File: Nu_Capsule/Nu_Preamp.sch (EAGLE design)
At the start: 27 parts, among them Q1 2SC3324, Q2 2SC3324, U1 TLV170

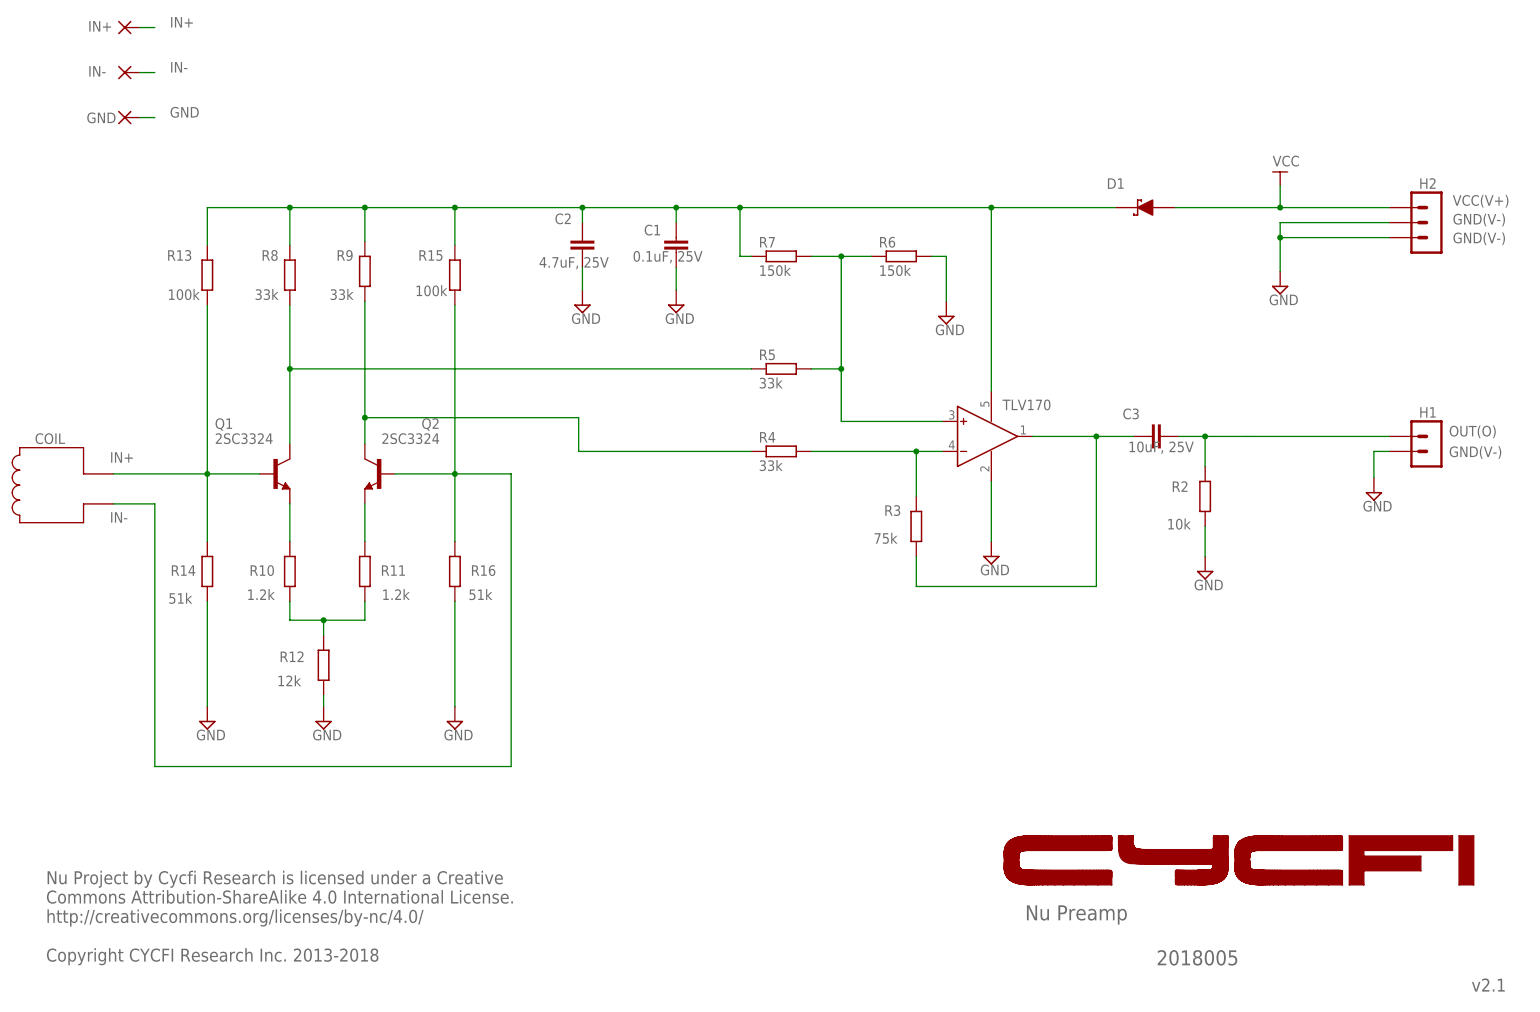
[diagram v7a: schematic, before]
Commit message: Remove commas and voltage rating on capacitor symbols on schematics
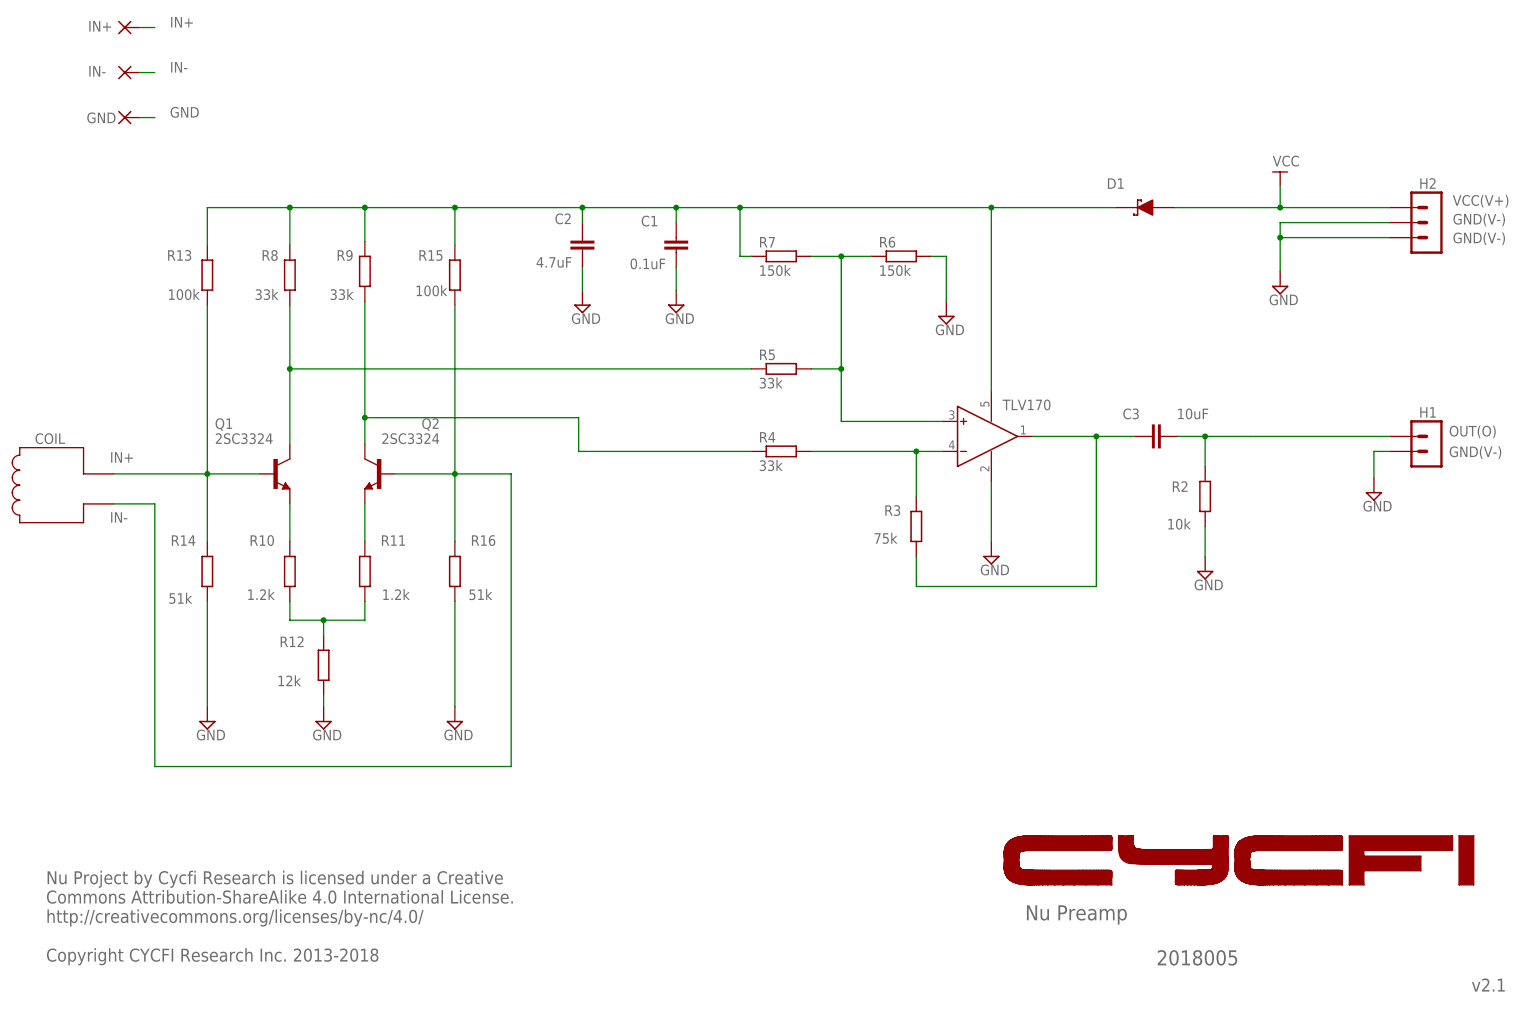
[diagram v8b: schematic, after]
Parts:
- C1: value 0.1uF, 25V -> 0.1uF
- C2: value 4.7uF, 25V -> 4.7uF
- C3: value 10uF, 25V -> 10uF
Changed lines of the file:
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@@
 <part name="SUPPLY10" library="supply2" deviceset="GND" device=""/>
 <part name="D1" library="m-pad-2.1" deviceset="D_SCHOTTKY" device="L"/>
-<part name="C1" library="rcl" deviceset="C-EU" device="C0402" value="0.1uF, 25V"/>
+<part name="C1" library="rcl" deviceset="C-EU" device="C0402" value="0.1uF"/>
 <part name="SUPPLY11" library="supply2" deviceset="GND" device=""/>
 <part name="SUPPLY12" library="supply2" deviceset="GND" device=""/>
@@
 <part name="SUPPLY15" library="supply2" deviceset="GND" device=""/>
 <part name="U1" library="CYCFI_semicon" deviceset="TLV170" device="" value="TLV170"/>
-<part name="C3" library="rcl" deviceset="C0603_NK" device="" value="10uF, 25V"/>
+<part name="C3" library="rcl" deviceset="C0603_NK" device="" value="10uF"/>
 <part name="H2" library="CYCFI_Con" deviceset="3P-2MM-TH-MALE" device=""/>
 <part name="H1" library="CYCFI_Con" deviceset="2P-2MM-TH-MALE" device=""/>
 <part name="SUPPLY1" library="supply2" deviceset="GND" device=""/>
-<part name="C2" library="rcl" deviceset="C0603_NK" device="" value="4.7uF, 25V"/>
+<part name="C2" library="rcl" deviceset="C0603_NK" device="" value="4.7uF"/>
 <part name="IN+" library="wirepad" deviceset="SMD2" device=""/>
 <part name="IN-" library="wirepad" deviceset="SMD2" device=""/>
@@
 </instance>
 <instance part="R10" gate="G$1" x="53.34" y="78.105" smashed="yes" rot="R90">
-<attribute name="NAME" x="50.8" y="79.1464" size="1.778" layer="95" rot="R180"/>
+<attribute name="NAME" x="50.8" y="84.2264" size="1.778" layer="95" rot="R180"/>
 <attribute name="VALUE" x="50.8" y="75.057" size="1.778" layer="96" rot="R180"/>
 </instance>
 <instance part="R11" gate="G$1" x="66.04" y="78.105" smashed="yes" rot="R90">
-<attribute name="NAME" x="73.025" y="79.1464" size="1.778" layer="95" rot="R180"/>
+<attribute name="NAME" x="73.025" y="84.2264" size="1.778" layer="95" rot="R180"/>
 <attribute name="VALUE" x="73.66" y="75.057" size="1.778" layer="96" rot="R180"/>
 </instance>
 <instance part="R12" gate="G$1" x="59.055" y="62.23" smashed="yes" rot="R90">
-<attribute name="NAME" x="55.88" y="64.5414" size="1.778" layer="95" rot="R180"/>
+<attribute name="NAME" x="55.88" y="67.0814" size="1.778" layer="95" rot="R180"/>
 <attribute name="VALUE" x="55.245" y="60.452" size="1.778" layer="96" rot="R180"/>
 </instance>
@@
 </instance>
 <instance part="R14" gate="G$1" x="39.37" y="78.105" smashed="yes" rot="R90">
-<attribute name="NAME" x="37.465" y="79.1464" size="1.778" layer="95" rot="R180"/>
+<attribute name="NAME" x="37.465" y="84.2264" size="1.778" layer="95" rot="R180"/>
 <attribute name="VALUE" x="36.83" y="74.422" size="1.778" layer="96" rot="R180"/>
 </instance>
@@
 </instance>
 <instance part="R16" gate="G$1" x="81.28" y="78.105" smashed="yes" rot="R90">
-<attribute name="NAME" x="88.265" y="79.1464" size="1.778" layer="95" rot="R180"/>
+<attribute name="NAME" x="88.265" y="84.2264" size="1.778" layer="95" rot="R180"/>
 <attribute name="VALUE" x="87.63" y="75.057" size="1.778" layer="96" rot="R180"/>
 </instance>
@@
 </instance>
 <instance part="C1" gate="G$1" x="118.745" y="134.62" smashed="yes">
-<attribute name="NAME" x="113.284" y="135.001" size="1.778" layer="95"/>
-<attribute name="VALUE" x="111.379" y="130.556" size="1.778" layer="96"/>
+<attribute name="NAME" x="112.776" y="136.525" size="1.778" layer="95"/>
+<attribute name="VALUE" x="110.871" y="129.286" size="1.778" layer="96"/>
 </instance>
 <instance part="SUPPLY11" gate="GND" x="102.87" y="123.19"/>
@@
 <instance part="C3" gate="G$1" x="198.755" y="100.965" smashed="yes" rot="R90">
 <attribute name="NAME" x="197.231" y="105.664" size="1.778" layer="95" rot="R180"/>
-<attribute name="VALUE" x="206.375" y="100.076" size="1.778" layer="96" rot="R180"/>
+<attribute name="VALUE" x="208.915" y="105.664" size="1.778" layer="96" rot="R180"/>
 </instance>
 <instance part="H2" gate="G$1" x="247.015" y="137.16" smashed="yes" rot="R180">
@@
 <instance part="C2" gate="G$1" x="102.87" y="132.08" smashed="yes" rot="R180">
 <attribute name="NAME" x="98.171" y="136.906" size="1.778" layer="95"/>
-<attribute name="VALUE" x="95.504" y="129.54" size="1.778" layer="96"/>
+<attribute name="VALUE" x="94.996" y="129.54" size="1.778" layer="96"/>
 </instance>
 <instance part="IN+" gate="1" x="25.4" y="170.18" smashed="yes">
